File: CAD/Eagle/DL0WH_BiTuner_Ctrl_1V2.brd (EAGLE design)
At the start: 96.5 x 73 mm, 145 parts, among them Q0321 ABS07-32.768KHZ, U0101 STM32L476RXT_64PIN_LDO, U0601 MC33996, U0701 MC33996, U0801 MC33996, U0921 TS5A23166, U0951 OPA354, U0961 OPA354, U1001 MAX232_SOIC16, U1101 MAX232_SOIC16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

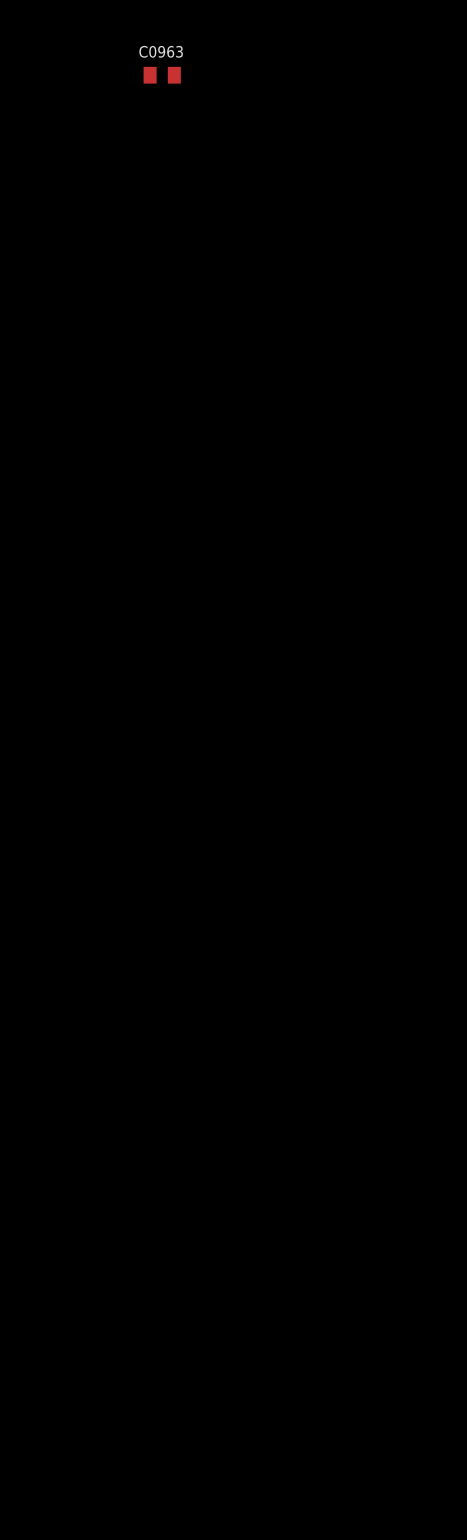
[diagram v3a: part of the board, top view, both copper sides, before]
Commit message: HW_1V2 - CAD/Eagle - LogAmp enhanced
Signed-off-by: Ulrich Habel <espero7757@gmx.net>
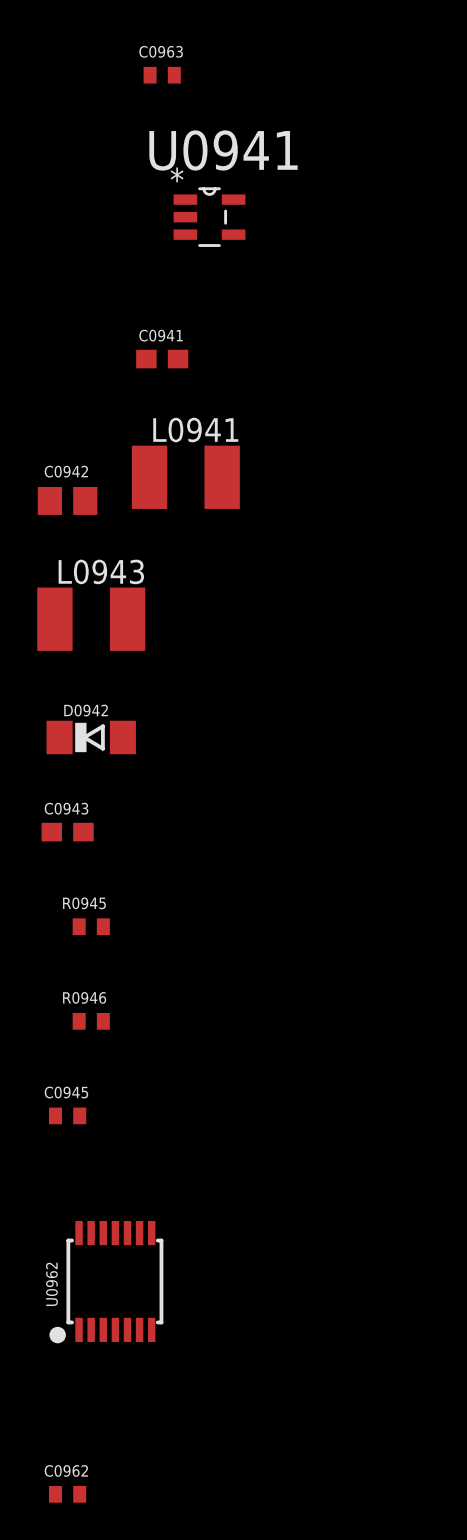
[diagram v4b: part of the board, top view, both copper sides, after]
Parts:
- added C0941, C0943: 22uF, df4iah_rcl:C0603
- added C0942: 2.2uF, df4iah_rcl:C0805
- added C0945: 1nF, df4iah_rcl:C0402
- added C0962: 100nF, df4iah_rcl:C0402
- added D0942: CRS08, df4iah_diode:SOD80C
- added L0941, L0943: 20uH, df4iah_rcl:L1812
- added R0945: 8.2kR, df4iah_rcl:R0402
- added R0946: 33kR, df4iah_rcl:R0402
- added U0941: LM2611, df4iah_powersupply:SOT95P280X145-5N
- added U0962: MCP4661-103E-MS, df4iah_dig-pot:TSSOP14
- R0962: value 4.7kR -> 1.0kR
- R0963: value 18kR -> 10kR
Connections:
- new net LM2611_NFB: C0945.1, R0945.1, R0946.2, U0941.3
- new net LM2611_SW: C0942.1, L0941.1, U0941.1
- new net LM_DA: C0942.2, D0942.A, L0943.2
- new net OPA_FB: R0963.1, U0962.7
- new net OPA_PULL: R0962.2, U0962.9
- net +3V3: now also C0941.1, C0962.1, L0941.2, U0941.4, U0941.5, U0962.11, U0962.14, U0962.8; no longer R0962.2
- net -1V5: now also C0943.1, C0945.2, L0943.1, R0945.2
- net GND: now also C0941.2, C0943.2, C0962.2, D0942.C, R0946.1, U0941.2, U0962.1, U0962.12, U0962.13, U0962.4
- net PB6: now also U0962.2
- net PB9: now also U0962.3
- net SWR_OP2_IN: now also U0962.6; no longer R0963.1
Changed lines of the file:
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@@
 </element>
 <element name="R0961" library="df4iah_rcl" package="R0402" value="1kR" x="-3.81" y="-39.37"/>
-<element name="R0962" library="df4iah_rcl" package="R0402" value="4.7kR" x="-3.81" y="-44.45"/>
-<element name="R0963" library="df4iah_rcl" package="R0402" value="18kR" x="-3.81" y="-49.53"/>
+<element name="R0962" library="df4iah_rcl" package="R0402" value="1.0kR" x="-3.81" y="-44.45"/>
+<element name="R0963" library="df4iah_rcl" package="R0402" value="10kR" x="-3.81" y="-49.53"/>
 <element name="C0963" library="df4iah_rcl" package="C0402" value="100pF" x="-3.81" y="-54.61"/>
+<element name="U0941" library="df4iah_powersupply" package="SOT95P280X145-5N" value="LM2611" x="-1.27" y="-62.23"/>
+<element name="C0941" library="df4iah_rcl" package="C0603" value="22uF" x="-3.81" y="-69.85"/>
+<element name="L0941" library="df4iah_rcl" package="L1812" value="20uH" x="-2.54" y="-76.2"/>
+<element name="C0942" library="df4iah_rcl" package="C0805" value="2.2uF" x="-8.89" y="-77.47"/>
+<element name="L0943" library="df4iah_rcl" package="L1812" value="20uH" x="-7.62" y="-83.82"/>
+<element name="D0942" library="df4iah_diode" package="SOD80C" value="CRS08" x="-7.62" y="-90.17"/>
+<element name="C0943" library="df4iah_rcl" package="C0603" value="22uF" x="-8.89" y="-95.25"/>
+<element name="R0945" library="df4iah_rcl" package="R0402" value="8.2kR" x="-7.62" y="-100.33"/>
+<element name="R0946" library="df4iah_rcl" package="R0402" value="33kR" x="-7.62" y="-105.41"/>
+<element name="C0945" library="df4iah_rcl" package="C0402" value="1nF" x="-8.89" y="-110.49"/>
+<element name="U0962" library="df4iah_dig-pot" package="TSSOP14" value="MCP4661-103E-MS" x="-6.35" y="-119.38"/>
+<element name="C0962" library="df4iah_rcl" package="C0402" value="100nF" x="-8.89" y="-130.81"/>
 </elements>
 <signals>
@@
 <contactref element="C0952" pad="2"/>
 <contactref element="U0961" pad="3"/>
-<wire x1="65.745" y1="56.72" x2="68.58" y2="58.42" width="0" layer="19" extent="1-1"/>
+<contactref element="C0941" pad="2"/>
+<contactref element="U0941" pad="2"/>
+<contactref element="D0942" pad="C"/>
+<contactref element="C0943" pad="2"/>
+<contactref element="R0946" pad="1"/>
+<contactref element="U0962" pad="4"/>
+<contactref element="U0962" pad="12"/>
+<contactref element="U0962" pad="13"/>
+<contactref element="U0962" pad="1"/>
+<contactref element="C0962" pad="2"/>
+<wire x1="-8.275" y1="-121.98" x2="-8.24" y2="-130.81" width="0" layer="19" extent="1-1"/>
+<wire x1="-6.325" y1="-121.98" x2="-8.275" y2="-121.98" width="0" layer="19" extent="1-1"/>
+<wire x1="-7.625" y1="-116.78" x2="-8.275" y2="-121.98" width="0" layer="19" extent="1-1"/>
+<wire x1="-6.975" y1="-116.78" x2="-7.625" y2="-116.78" width="0" layer="19" extent="1-1"/>
+<wire x1="-8.27" y1="-105.41" x2="-7.625" y2="-116.78" width="0" layer="19" extent="1-1"/>
+<wire x1="-8.04" y1="-95.25" x2="-8.27" y2="-105.41" width="0" layer="19" extent="1-1"/>
+<wire x1="-9.32" y1="-90.17" x2="-8.04" y2="-95.25" width="0" layer="19" extent="1-1"/>
+<wire x1="-2.96" y1="-69.85" x2="-9.32" y2="-90.17" width="0" layer="19" extent="1-1"/>
+<wire x1="-2.5654" y1="-62.23" x2="-2.96" y2="-69.85" width="0" layer="19" extent="1-1"/>
+<wire x1="-2.5654" y1="-32.6898" x2="-2.5654" y2="-62.23" width="0" layer="19" extent="1-1"/>
+<wire x1="-3.16" y1="-24.13" x2="-2.5654" y2="-32.6898" width="0" layer="19" extent="1-1"/>
+<wire x1="6.35" y1="1.27" x2="-3.16" y2="-24.13" width="0" layer="19" extent="1-16"/>
 <wire x1="15.3875" y1="53.295" x2="14.2875" y2="53.295" width="0" layer="19" extent="1-1"/>
 <wire x1="13.1875" y1="53.295" x2="14.2875" y2="53.295" width="0" layer="19" extent="1-1"/>
@@
 <wire x1="13.1875" y1="57.195" x2="14.2875" y2="57.195" width="0" layer="19" extent="1-1"/>
 <wire x1="55.88" y1="20.32" x2="57.62625" y2="18.0825" width="0" layer="19" extent="1-1"/>
+<wire x1="68.58" y1="58.42" x2="65.745" y2="56.72" width="0" layer="19" extent="1-1"/>
 <wire x1="17.62125" y1="26.51125" x2="14.605" y2="28.2575" width="0" layer="19" extent="1-1"/>
 <wire x1="68.8975" y1="26.51125" x2="65.3375" y2="27.21375" width="0" layer="19" extent="1-1"/>
 <wire x1="10.16" y1="33.02" x2="13.97" y2="31.75" width="0" layer="19" extent="16-16"/>
-<wire x1="-3.16" y1="-24.13" x2="6.35" y2="1.27" width="0" layer="19" extent="1-16"/>
-<wire x1="-2.5654" y1="-32.6898" x2="-3.16" y2="-24.13" width="0" layer="19" extent="1-1"/>
 </signal>
 <signal name="VDDUSB">
@@
 <wire x1="79.375" y1="3.81" x2="80.01" y2="4.445" width="0.3048" layer="16"/>
 <contactref element="U0961" pad="5"/>
-<contactref element="R0962" pad="2"/>
-<wire x1="0.0254" y1="-30.8102" x2="-3.16" y2="-44.45" width="0" layer="19" extent="1-1"/>
+<contactref element="U0941" pad="5"/>
+<contactref element="U0941" pad="4"/>
+<contactref element="C0941" pad="1"/>
+<contactref element="L0941" pad="2"/>
+<contactref element="U0962" pad="8"/>
+<contactref element="U0962" pad="14"/>
+<contactref element="U0962" pad="11"/>
+<contactref element="C0962" pad="1"/>
+<wire x1="-8.275" y1="-116.78" x2="-9.54" y2="-130.81" width="0" layer="19" extent="1-1"/>
+<wire x1="-6.325" y1="-116.78" x2="-8.275" y2="-116.78" width="0" layer="19" extent="1-1"/>
+<wire x1="-4.375" y1="-116.78" x2="-6.325" y2="-116.78" width="0" layer="19" extent="1-1"/>
+<wire x1="-0.59" y1="-76.2" x2="-4.375" y2="-116.78" width="0" layer="19" extent="1-1"/>
+<wire x1="-4.66" y1="-69.85" x2="-0.59" y2="-76.2" width="0" layer="19" extent="1-1"/>
+<wire x1="0.0254" y1="-63.1698" x2="-4.66" y2="-69.85" width="0" layer="19" extent="1-1"/>
+<wire x1="0.0254" y1="-61.2902" x2="0.0254" y2="-63.1698" width="0" layer="19" extent="1-1"/>
+<wire x1="0.0254" y1="-30.8102" x2="0.0254" y2="-61.2902" width="0" layer="19" extent="1-1"/>
 <wire x1="8.5725" y1="23.8125" x2="0.0254" y2="-30.8102" width="0" layer="19" extent="1-1"/>
 <wire x1="8.255" y1="24.335" x2="8.5725" y2="23.8125" width="0" layer="19" extent="1-1"/>
@@
 <wire x1="69.215" y1="27.94" x2="67.8375" y2="26.5625" width="0.1524" layer="1"/>
 <wire x1="67.83" y1="24.825" x2="67.8375" y2="26.5625" width="0.1524" layer="1"/>
+<contactref element="U0962" pad="2"/>
+<wire x1="67.83" y1="24.825" x2="-7.625" y2="-121.98" width="0" layer="19" extent="1-1"/>
 </signal>
 <signal name="PB7">
@@
 <wire x1="69.85" y1="27.305" x2="71.4225" y2="27.305" width="0.1524" layer="1"/>
 <wire x1="71.4225" y1="27.305" x2="71.4375" y2="27.29" width="0.1524" layer="1"/>
+<contactref element="U0962" pad="3"/>
+<wire x1="65.83" y1="24.825" x2="-6.975" y2="-121.98" width="0" layer="19" extent="1-1"/>
 </signal>
 <signal name="PB10" class="6">
@@
 <contactref element="C0952" pad="1"/>
 <contactref element="U0961" pad="2"/>
-<wire x1="-4.46" y1="-24.13" x2="12.7" y2="24.7396" width="0" layer="19" extent="1-16"/>
-<wire x1="-2.5654" y1="-31.75" x2="-4.46" y2="-24.13" width="0" layer="19" extent="1-1"/>
+<contactref element="L0943" pad="1"/>
+<contactref element="C0943" pad="1"/>
+<contactref element="R0945" pad="2"/>
+<contactref element="C0945" pad="2"/>
+<wire x1="-6.97" y1="-100.33" x2="-8.24" y2="-110.49" width="0" layer="19" extent="1-1"/>
+<wire x1="-9.74" y1="-95.25" x2="-6.97" y2="-100.33" width="0" layer="19" extent="1-1"/>
+<wire x1="-9.57" y1="-83.82" x2="-9.74" y2="-95.25" width="0" layer="19" extent="1-1"/>
+<wire x1="-2.5654" y1="-31.75" x2="-9.57" y2="-83.82" width="0" layer="19" extent="1-1"/>
+<wire x1="-4.46" y1="-24.13" x2="-2.5654" y2="-31.75" width="0" layer="19" extent="1-1"/>
+<wire x1="12.7" y1="24.7396" x2="-4.46" y2="-24.13" width="0" layer="19" extent="1-16"/>
 </signal>
 <signal name="SWR_OP2_IN">
@@
 <contactref element="U0961" pad="4"/>
 <contactref element="R0962" pad="1"/>
-<contactref element="R0963" pad="1"/>
 <contactref element="C0963" pad="1"/>
-<wire x1="-4.46" y1="-49.53" x2="-4.46" y2="-54.61" width="0" layer="19" extent="1-1"/>
-<wire x1="-4.46" y1="-44.45" x2="-4.46" y2="-49.53" width="0" layer="19" extent="1-1"/>
+<contactref element="U0962" pad="6"/>
+<wire x1="-4.46" y1="-54.61" x2="-5.025" y2="-121.98" width="0" layer="19" extent="1-1"/>
+<wire x1="-4.46" y1="-44.45" x2="-4.46" y2="-54.61" width="0" layer="19" extent="1-1"/>
 <wire x1="-3.16" y1="-39.37" x2="-4.46" y2="-44.45" width="0" layer="19" extent="1-1"/>
 <wire x1="0.0254" y1="-32.6898" x2="-3.16" y2="-39.37" width="0" layer="19" extent="1-1"/>
@@
 <wire x1="14.59" y1="22.86" x2="-2.5654" y2="-30.8102" width="0" layer="19" extent="1-16"/>
 </signal>
+<signal name="LM2611_SW">
+<contactref element="L0941" pad="1"/>
+<contactref element="U0941" pad="1"/>
+<contactref element="C0942" pad="1"/>
+<wire x1="-4.49" y1="-76.2" x2="-9.84" y2="-77.47" width="0" layer="19" extent="1-1"/>
+<wire x1="-2.5654" y1="-61.2902" x2="-4.49" y2="-76.2" width="0" layer="19" extent="1-1"/>
+</signal>
+<signal name="LM_DA">
+<contactref element="C0942" pad="2"/>
+<contactref element="L0943" pad="2"/>
+<contactref element="D0942" pad="A"/>
+<wire x1="-5.67" y1="-83.82" x2="-5.92" y2="-90.17" width="0" layer="19" extent="1-1"/>
+<wire x1="-7.94" y1="-77.47" x2="-5.67" y2="-83.82" width="0" layer="19" extent="1-1"/>
+</signal>
+<signal name="LM2611_NFB">
+<contactref element="U0941" pad="3"/>
+<contactref element="R0946" pad="2"/>
+<contactref element="R0945" pad="1"/>
+<contactref element="C0945" pad="1"/>
+<wire x1="-6.97" y1="-105.41" x2="-9.54" y2="-110.49" width="0" layer="19" extent="1-1"/>
+<wire x1="-8.27" y1="-100.33" x2="-6.97" y2="-105.41" width="0" layer="19" extent="1-1"/>
+<wire x1="-2.5654" y1="-63.1698" x2="-8.27" y2="-100.33" width="0" layer="19" extent="1-1"/>
+</signal>
+<signal name="OPA_PULL">
+<contactref element="R0962" pad="2"/>
+<contactref element="U0962" pad="9"/>
+<wire x1="-3.16" y1="-44.45" x2="-5.025" y2="-116.78" width="0" layer="19" extent="1-1"/>
+</signal>
+<signal name="OPA_FB">
+<contactref element="R0963" pad="1"/>
+<contactref element="U0962" pad="7"/>
+<wire x1="-4.46" y1="-49.53" x2="-4.375" y2="-121.98" width="0" layer="19" extent="1-1"/>
+</signal>
 </signals>
